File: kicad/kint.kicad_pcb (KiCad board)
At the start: 2 copper layers, 107.9 x 86 mm, 27 parts, among them J1 THUMB_RIGHT_SPC_KB600, J2 LEFT_13_LT, J3 TOP_LEFT, J4 TOP_RIGHT, J5 THUMB_LEFT_BAK, J6 THUMB_RIGHT_SPC, J7 RIGHT_13_DOWN, J8 THUMB_LEFT_BAK_KB600, U1 TEENSY_3.5_3.6

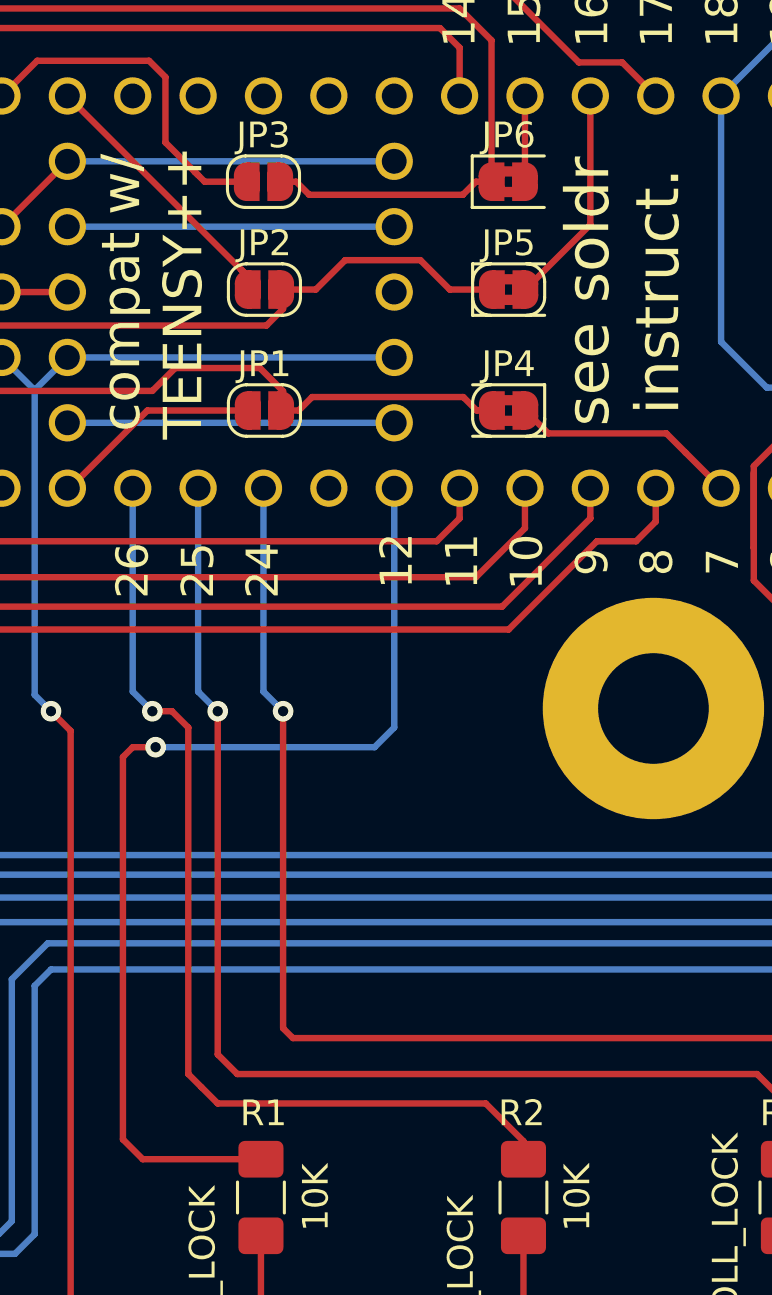
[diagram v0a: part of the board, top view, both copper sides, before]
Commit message: Update to Kicad 6.0
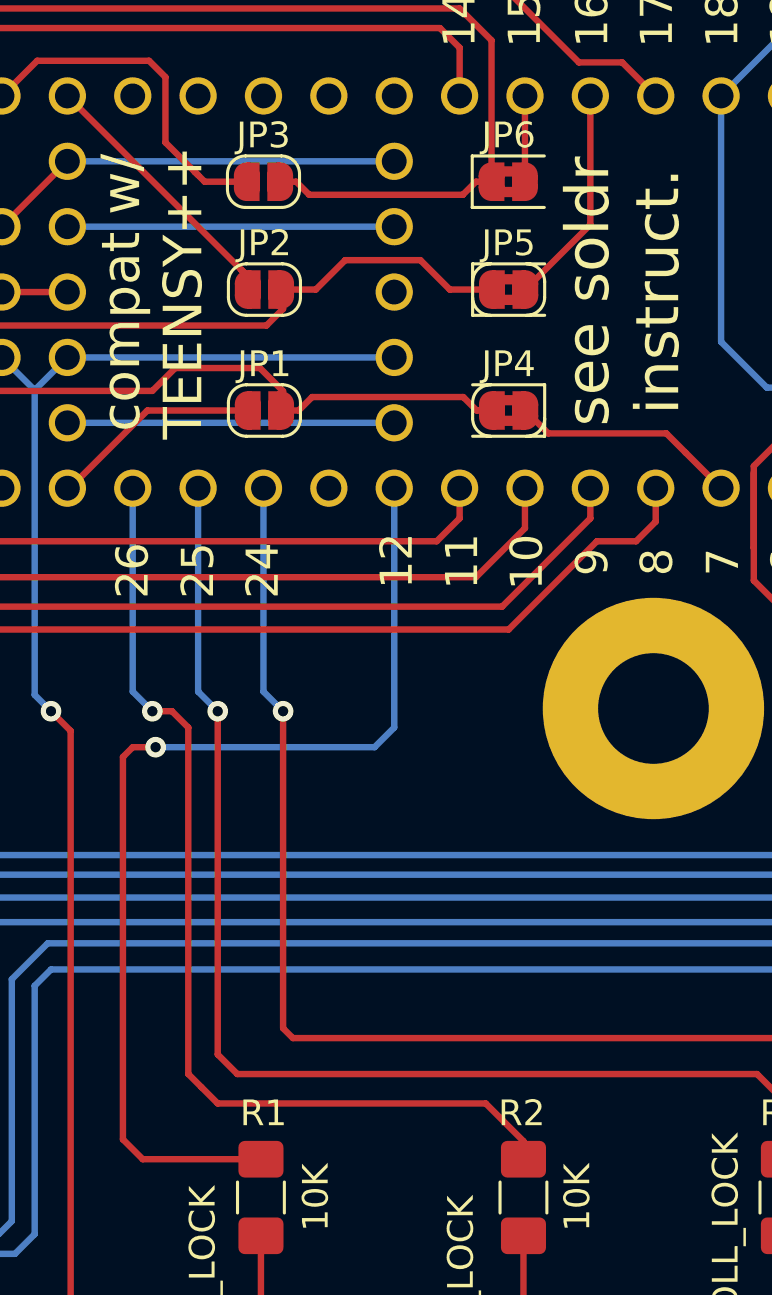
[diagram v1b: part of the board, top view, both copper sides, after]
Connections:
- JP1 pad 1: Net-(JP1-Pad1) -> (no net)
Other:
- net class Default removed
